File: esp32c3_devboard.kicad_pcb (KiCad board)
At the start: 2 copper layers, 50 x 30 mm, 37 parts, among them J1 UART USB, J2 JTAG USB, J3 Conn_01x15_Male, J4 Conn_01x15_Male, U1 ESP32-C3-MINI-1, U2 SRV05-4, U3 AMS1117-3.3, U4 CP2102N-A01-GQFN28

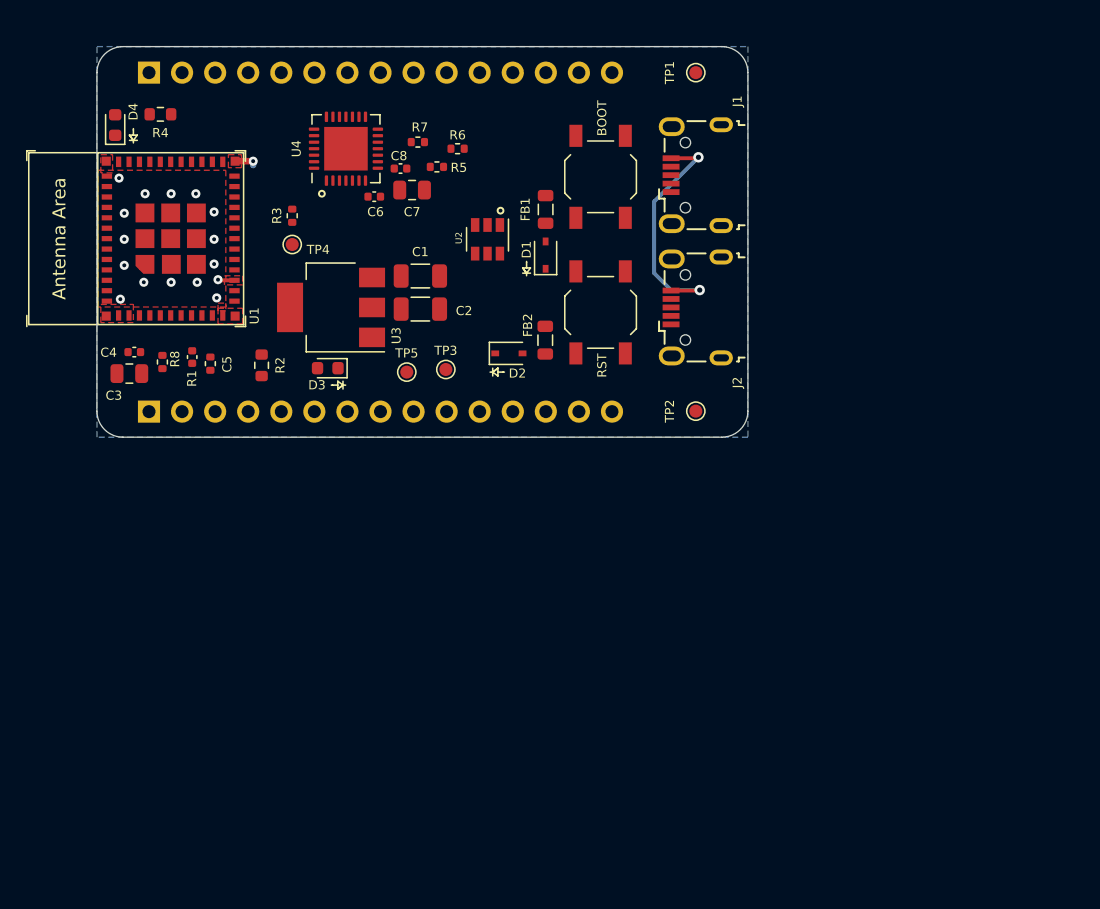
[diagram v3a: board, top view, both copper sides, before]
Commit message: Add Microchip USB2514Bi USB hub to schematic and PCB
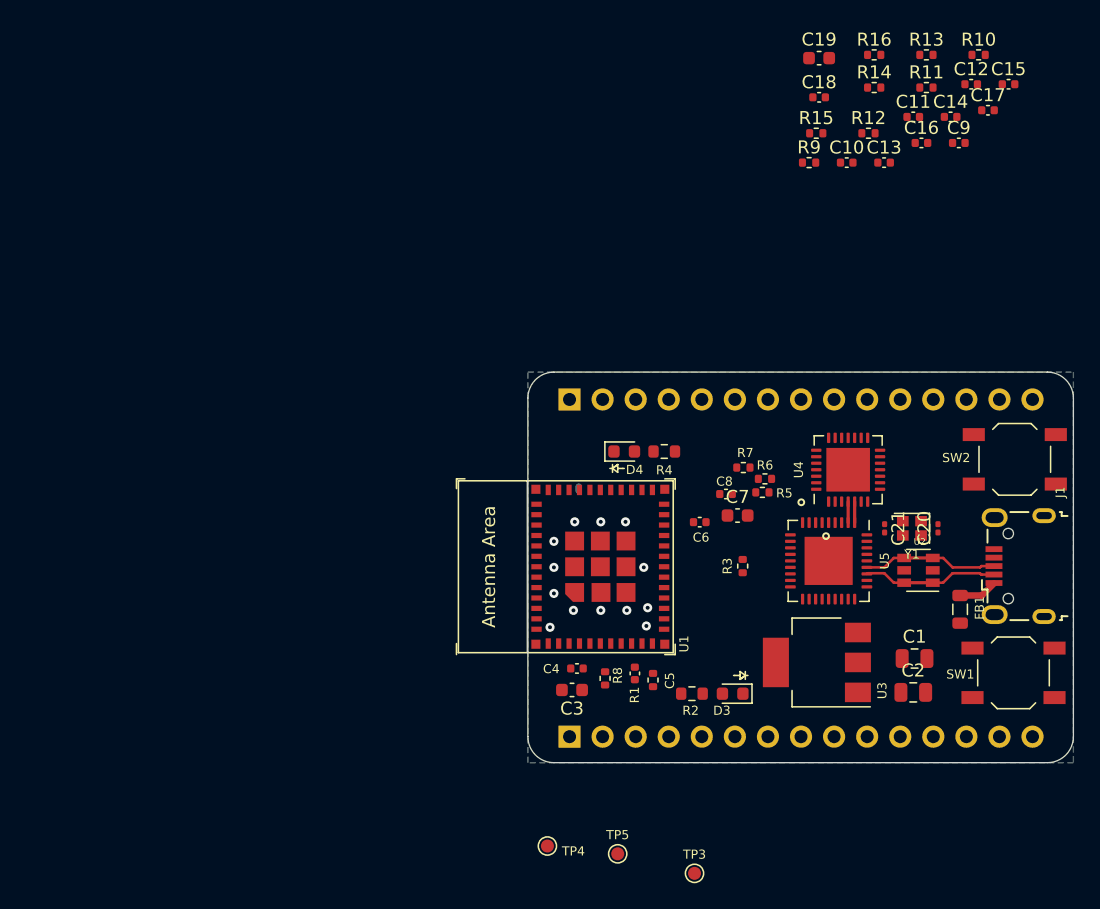
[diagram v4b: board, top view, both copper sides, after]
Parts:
- removed D1, D2: D_Schottky, Diode_SMD:D_SOD-323
- removed FB2: 100Ω @ 100MHz, Inductor_SMD:L_0805_2012Metric
- removed J2: JTAG USB, Connector_USB:USB_Micro-B_Wuerth_629105150521
- removed TP1: TP_5V_UART_USB, TestPoint:TestPoint_Pad_D1.0mm
- removed TP2: TP_5V_JTAG_USB, TestPoint:TestPoint_Pad_D1.0mm
- added C10: 100n, Capacitor_SMD:C_0402_1005Metric, F.Cu at (157.6, 68.9)
- added C11: 100n, Capacitor_SMD:C_0402_1005Metric, F.Cu at (162.7, 65.4)
- added C12: 100n, Capacitor_SMD:C_0402_1005Metric, F.Cu at (167.2, 62.9)
- added C13: 100n, Capacitor_SMD:C_0402_1005Metric, F.Cu at (160.5, 68.9)
- added C14: 100n, Capacitor_SMD:C_0402_1005Metric, F.Cu at (165.6, 65.4)
- added C15: 100n, Capacitor_SMD:C_0402_1005Metric, F.Cu at (170.0, 62.9)
- added C16: 100n, Capacitor_SMD:C_0402_1005Metric, F.Cu at (163.3, 67.4)
- added C17: 100n, Capacitor_SMD:C_0402_1005Metric, F.Cu at (168.4, 64.9)
- added C18: 100n, Capacitor_SMD:C_0402_1005Metric, F.Cu at (155.5, 63.9)
- added C19: 4.7u, Capacitor_SMD:C_0603_1608Metric, F.Cu at (155.5, 60.9)
- added C20: 18p, Capacitor_SMD:C_0201_0603Metric, F.Cu at (164.6, 97.0)
- added C21: 18p, Capacitor_SMD:C_0201_0603Metric, F.Cu at (160.5, 97.0)
- added C9: 1u, Capacitor_SMD:C_0402_1005Metric, F.Cu at (166.2, 67.4)
- added R10: 100K, Resistor_SMD:R_0402_1005Metric, F.Cu at (167.7, 60.6)
- added R11: 100K, Resistor_SMD:R_0402_1005Metric, F.Cu at (163.7, 63.1)
- added R12: 100K, Resistor_SMD:R_0402_1005Metric, F.Cu at (159.3, 66.7)
- added R13: 12K, Resistor_SMD:R_0402_1005Metric, F.Cu at (163.7, 60.6)
- added R14: 100K, Resistor_SMD:R_0402_1005Metric, F.Cu at (159.7, 63.1)
- added R15: 100K, Resistor_SMD:R_0402_1005Metric, F.Cu at (155.2, 66.7)
- added R16: 100K, Resistor_SMD:R_0402_1005Metric, F.Cu at (159.7, 60.6)
- added R9: 100K, Resistor_SMD:R_0402_1005Metric, F.Cu at (154.7, 68.9)
- added U5: USB2514B_Bi, Package_DFN_QFN:QFN-36-1EP_6x6mm_P0.5mm_EP3.7x3.7mm, F.Cu at (156.2, 99.5)
- added Y1: 24MHz, Crystal:Crystal_SMD_2016-4Pin_2.0x1.6mm, F.Cu at (162.6, 97.0)
- C1, C2: footprint Capacitor_SMD:C_1206_3216Metric -> Capacitor_SMD:C_0805_2012Metric
- C3, C7: footprint Capacitor_SMD:C_0805_2012Metric -> Capacitor_SMD:C_0603_1608Metric
- J1: value UART USB -> Micro_USB
- SW1: renamed from RST; value RSTN_SW -> RST
- SW2: renamed from BOOT; value USR_SW -> BOOT
- moved TP4 50.2 mm to (134.6, 121.4)
- moved C1 48.0 mm to (162.8, 107.0)
- moved C2 48.0 mm to (162.7, 109.6)
- moved R4 46.6 mm to (143.6, 91.1)
- moved D4 46.4 mm to (140.5, 91.1), turned to 0 degrees
- moved U3 46.2 mm to (155.3, 107.3)
- moved U4 45.8 mm to (157.7, 92.5)
- moved FB1 44.2 mm to (166.3, 103.2)
- moved R3 43.8 mm to (149.6, 99.9)
- moved TP3 43.2 mm to (145.9, 123.5)
- moved SW1 42.1 mm to (170.4, 108.1), turned to 180 degrees
- moved C4 41.8 mm to (136.9, 107.8)
- moved C3 41.8 mm to (136.5, 109.4)
- moved C5 41.8 mm to (141.3, 108.1)
- moved R8 41.8 mm to (139.0, 108.5)
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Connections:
- net +5VP renamed /5V_UP_USB
- FB1 pad 1: /5V_UART_USB_FLT -> +5V
- J1 pad 2: UART_USB_D- -> UP_USB_D-
- J1 pad 3: UART_USB_D+ -> UP_USB_D+
- R5 pad 1: /5V_UART_USB_FLT -> +5V
- U2 pad 1: UART_USB_D- -> UP_USB_D-
- U2 pad 3: UART_USB_D+ -> UP_USB_D+
- U2 pad 4: JTAG_USB_D- -> UP_USB_D+
- U2 pad 6: JTAG_USB_D+ -> UP_USB_D-
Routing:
- net GND: track 21.3 -> 0.53 mm, vias 19 -> 13
- net UP_USB_D-: track 0.00 -> 10.8 mm
- net UP_USB_D+: track 0.00 -> 10.8 mm
- net /5V_UP_USB: track 0.00 -> 2.99 mm
- net UART_USB_D-: track 0.00 -> 1.61 mm
- net UART_USB_D+: track 0.00 -> 1.61 mm
- removed copper zone on F.Cu, net GND
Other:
- board size 50 x 30 mm -> 41.9 x 30 mm

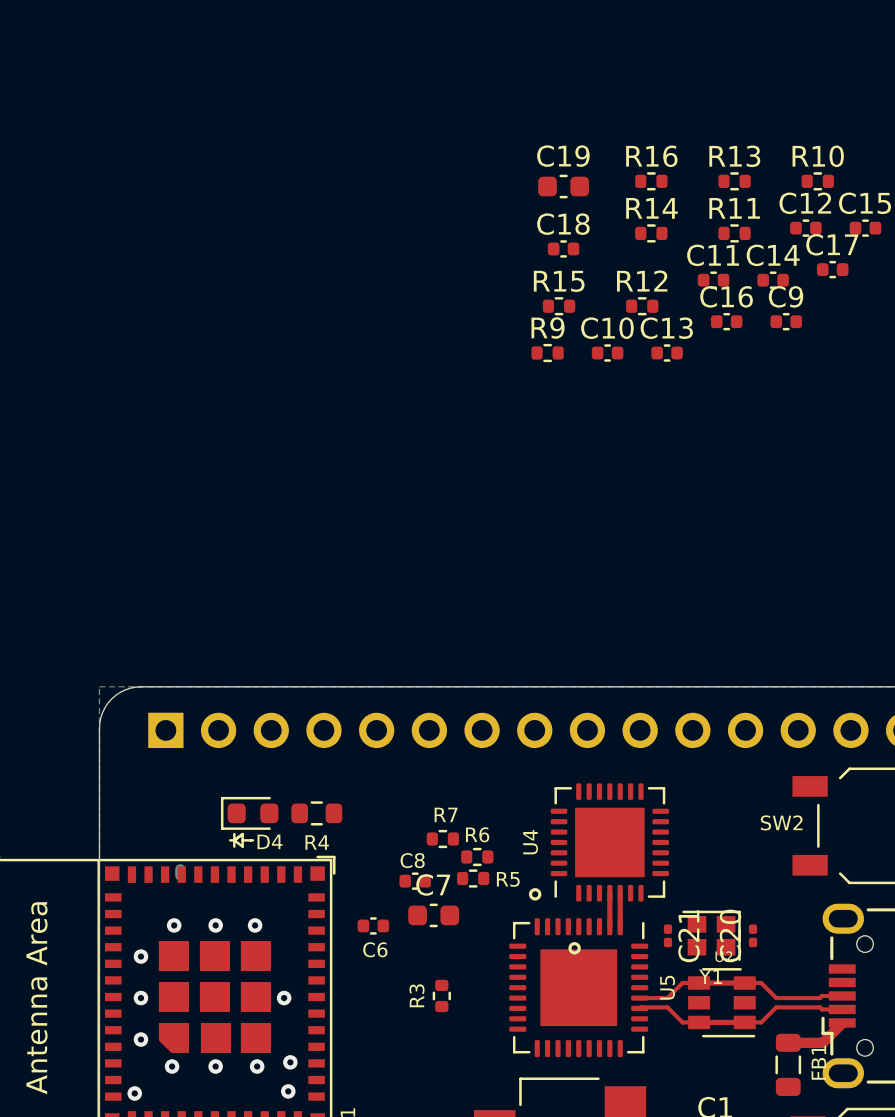
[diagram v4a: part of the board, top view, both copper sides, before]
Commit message: Configure bootstrapping pins on USB hub IC
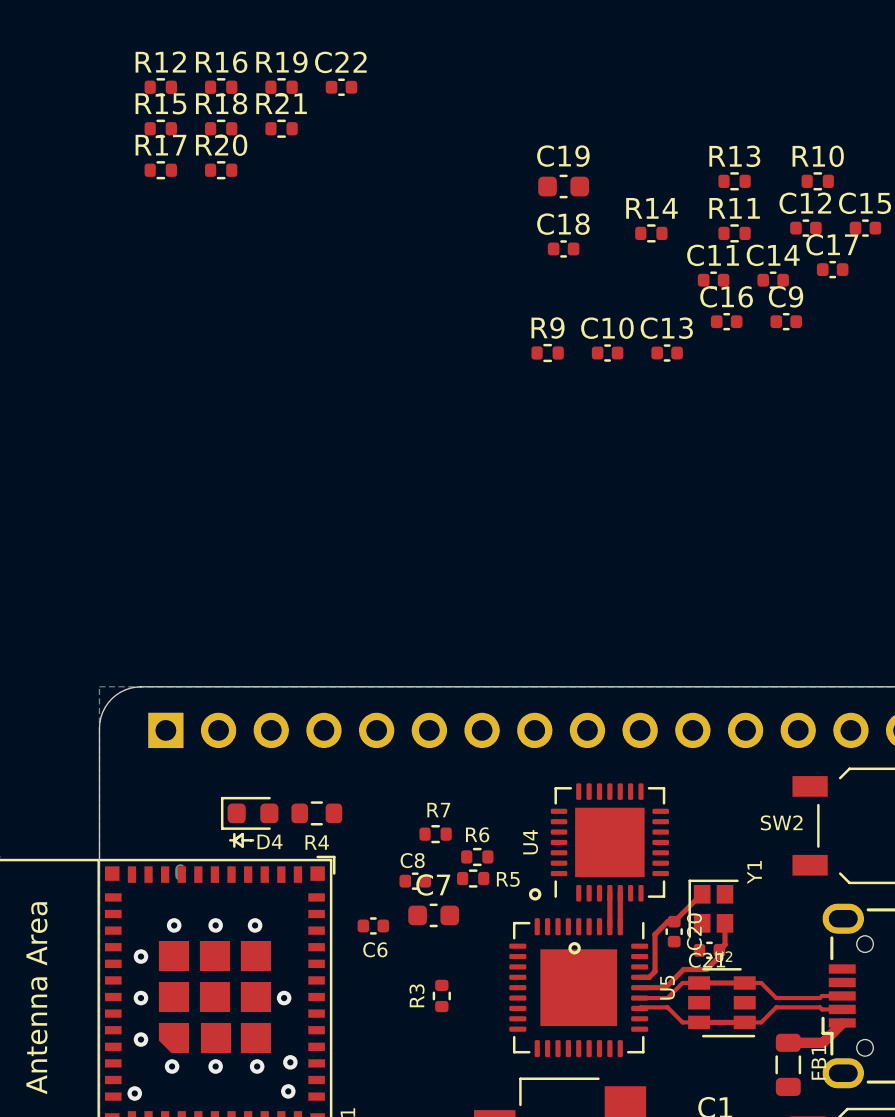
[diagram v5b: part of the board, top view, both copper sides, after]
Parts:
- added C22: 100n, Capacitor_SMD:C_0402_1005Metric, F.Cu at (144.8, 56.1)
- added R17: 330R, Resistor_SMD:R_0402_1005Metric, F.Cu at (136.1, 60.1)
- added R18: 10K, Resistor_SMD:R_0402_1005Metric, F.Cu at (139.0, 58.1)
- added R19: 10K, Resistor_SMD:R_0402_1005Metric, F.Cu at (141.9, 56.1)
- added R20: 10K, Resistor_SMD:R_0402_1005Metric, F.Cu at (139.0, 60.1)
- added R21: 10K, Resistor_SMD:R_0402_1005Metric, F.Cu at (141.9, 58.1)
- C10: value 100n -> 220n
- C19: value 4.7u -> 1u
- C20, C21: footprint Capacitor_SMD:C_0201_0603Metric -> Capacitor_SMD:C_0402_1005Metric
- R12, R15: value 100K -> 10K
- R13: value 12K -> 12K,1%
- moved R12 25.5 mm to (136.1, 56.1)
- moved R16 21.2 mm to (139.0, 56.1)
- moved R15 21.0 mm to (136.1, 58.1)
- moved C20 3.81 mm to (160.8, 96.8)
- moved C21 2.12 mm to (162.5, 97.7), turned to 0 degrees
- moved Y1 1.30 mm to (162.7, 95.7), turned to 270 degrees
- moved R7 0.42 mm to (149.3, 92.1)
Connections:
- R10 pad 1: Net-(R10-Pad1) -> GND
- R10 pad 2: GND -> CFG_SEL0
- R11 pad 1: +5V -> Net-(R11-Pad1)
- R11 pad 2: Net-(R11-Pad2) -> +5V
- R12 pad 1: Net-(R12-Pad1) -> +3V3
- R12 pad 2: GND -> CFG_SEL1
- R14 pad 1: Net-(R11-Pad2) -> Net-(R11-Pad1)
- R15 pad 1: Net-(R15-Pad1) -> +3V3
- R15 pad 2: GND -> NON_REM1
- R16 pad 1: Net-(R16-Pad1) -> GND
- R16 pad 2: GND -> NON_REM0
- U5 pad 22: Net-(R12-Pad1) -> NON_REM1
- U5 pad 24: Net-(R10-Pad1) -> CFG_SEL0
- U5 pad 25: Net-(R16-Pad1) -> CFG_SEL1
- U5 pad 27: Net-(R11-Pad2) -> Net-(R11-Pad1)
- U5 pad 28: Net-(R15-Pad1) -> NON_REM0
- U5 pad 6: +3V3 -> Net-(R18-Pad1)
- U5 pad 7: +3V3 -> Net-(R20-Pad1)
- U5 pad 8: +3V3 -> Net-(R19-Pad1)
- U5 pad 9: +3V3 -> Net-(R21-Pad1)
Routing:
- net USB_XTALOUT: track 0.00 -> 6.18 mm
- net USB_XTALIN: track 0.00 -> 5.72 mm
